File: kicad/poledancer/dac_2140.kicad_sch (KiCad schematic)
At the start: 16 parts, among them U7 AD5328

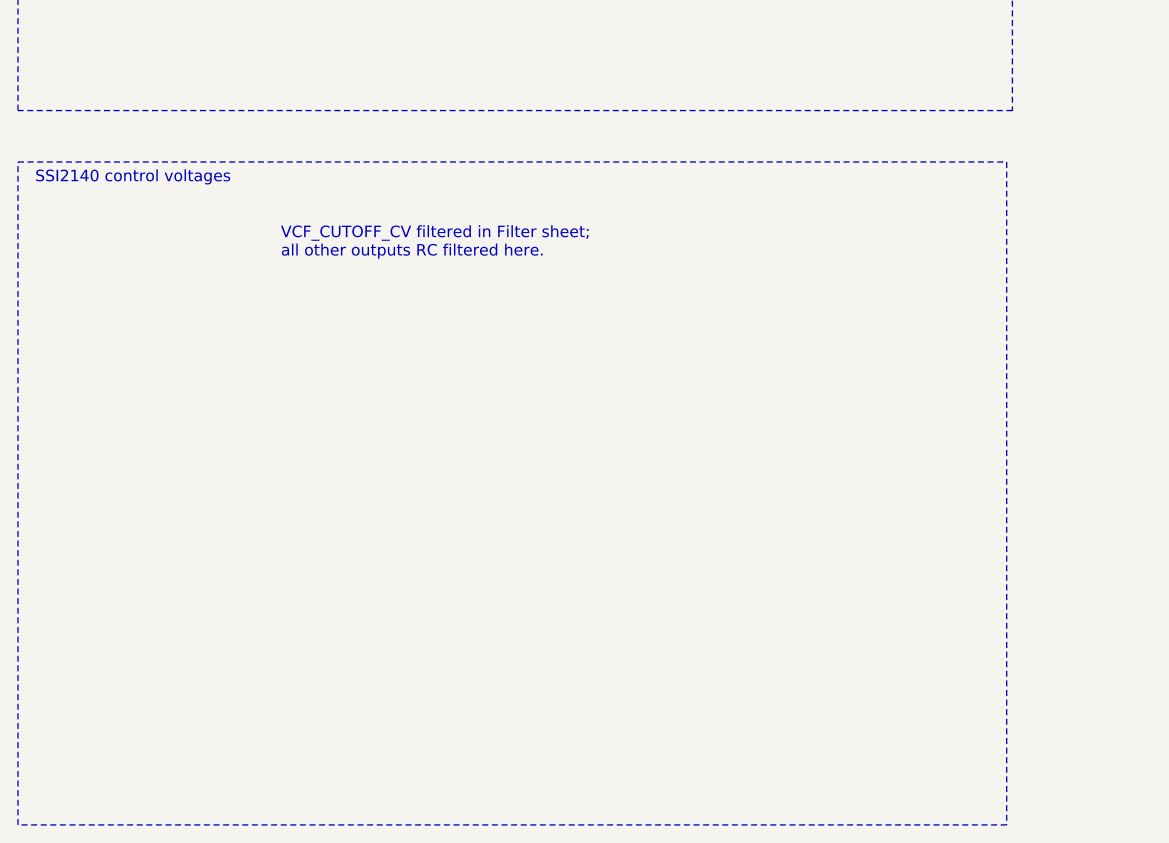
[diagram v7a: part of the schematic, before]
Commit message: renaming some DAC stuff
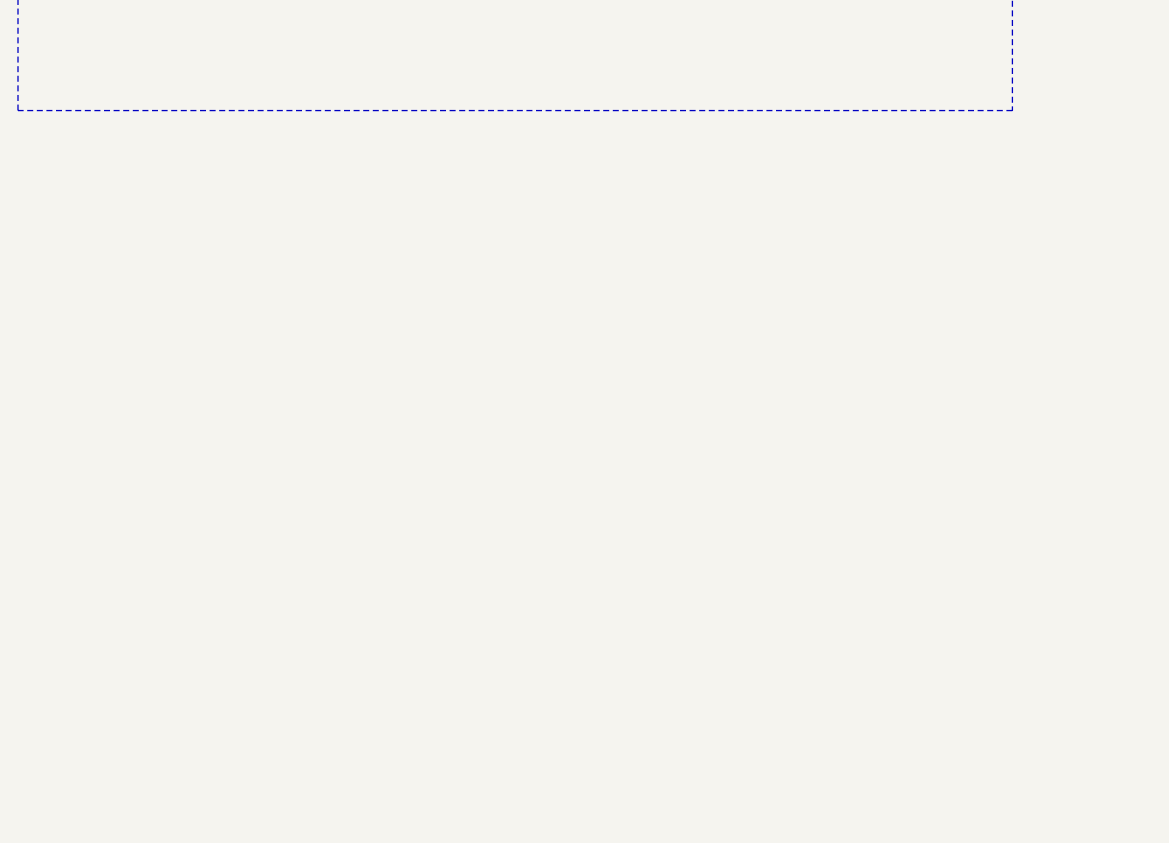
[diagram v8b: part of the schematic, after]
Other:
- note removed: "SSI2140 control voltages"
- note removed: "VCF_CUTOFF_CV filtered in Filter sheet; all other outputs RC filtered here."
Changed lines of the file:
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@@
-    (fill (type none))
-  )
-  (rectangle (start 22.86 102.235) (end 132.715 175.895)
-    (stroke (width 0) (type dash))
     (fill (type none))
   )
@@
     (effects (font (size 1.27 1.27)) (justify left bottom))
   )
-  (text "VCF_CUTOFF_CV filtered in Filter sheet;\nall other outputs RC filtered here."
-    (at 52.07 113.03 0)
-    (effects (font (size 1.27 1.27)) (justify left bottom))
-  )
   (text "DAC: 2.5V Reference Voltage\nB grade or better.\nAD5328: B version."
     (at 25.4 29.21 0)
     (effects (font (size 1.27 1.27)) (justify left bottom))
   )
-  (text "SSI2140 control voltages" (at 24.765 104.775 0)
-    (effects (font (size 1.27 1.27)) (justify left bottom))
-  )
